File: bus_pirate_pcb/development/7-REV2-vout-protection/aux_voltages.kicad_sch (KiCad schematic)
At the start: 11 parts, among them U18 74LVC2G14

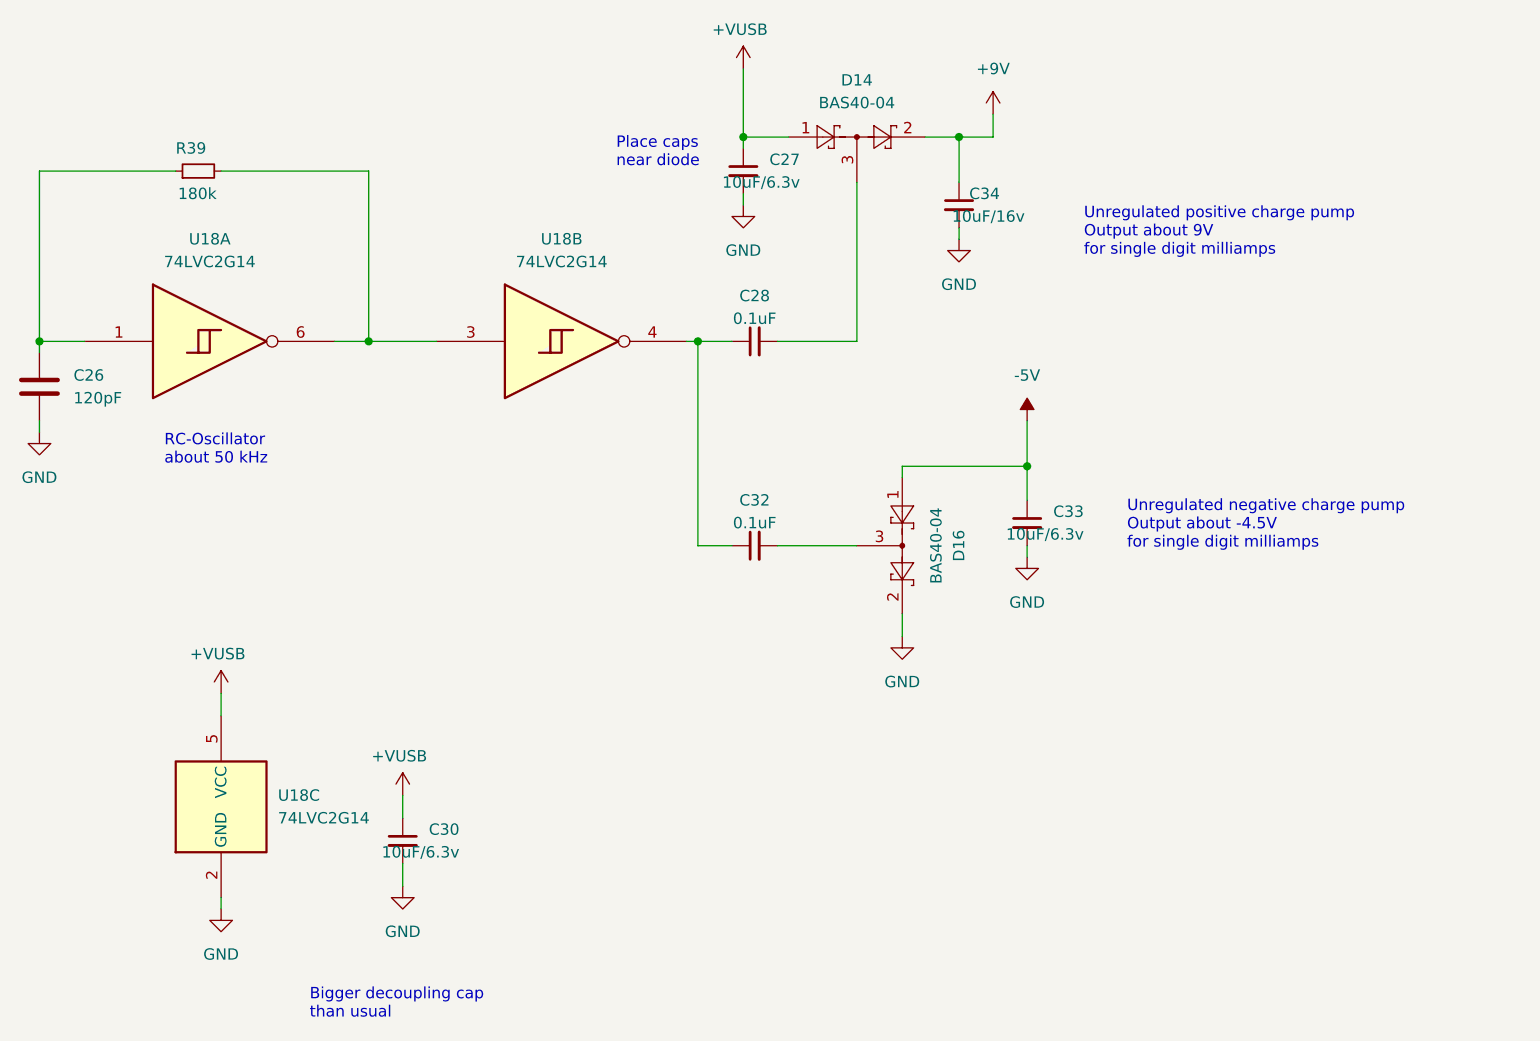
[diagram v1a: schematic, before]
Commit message: 7R2 with vout protection
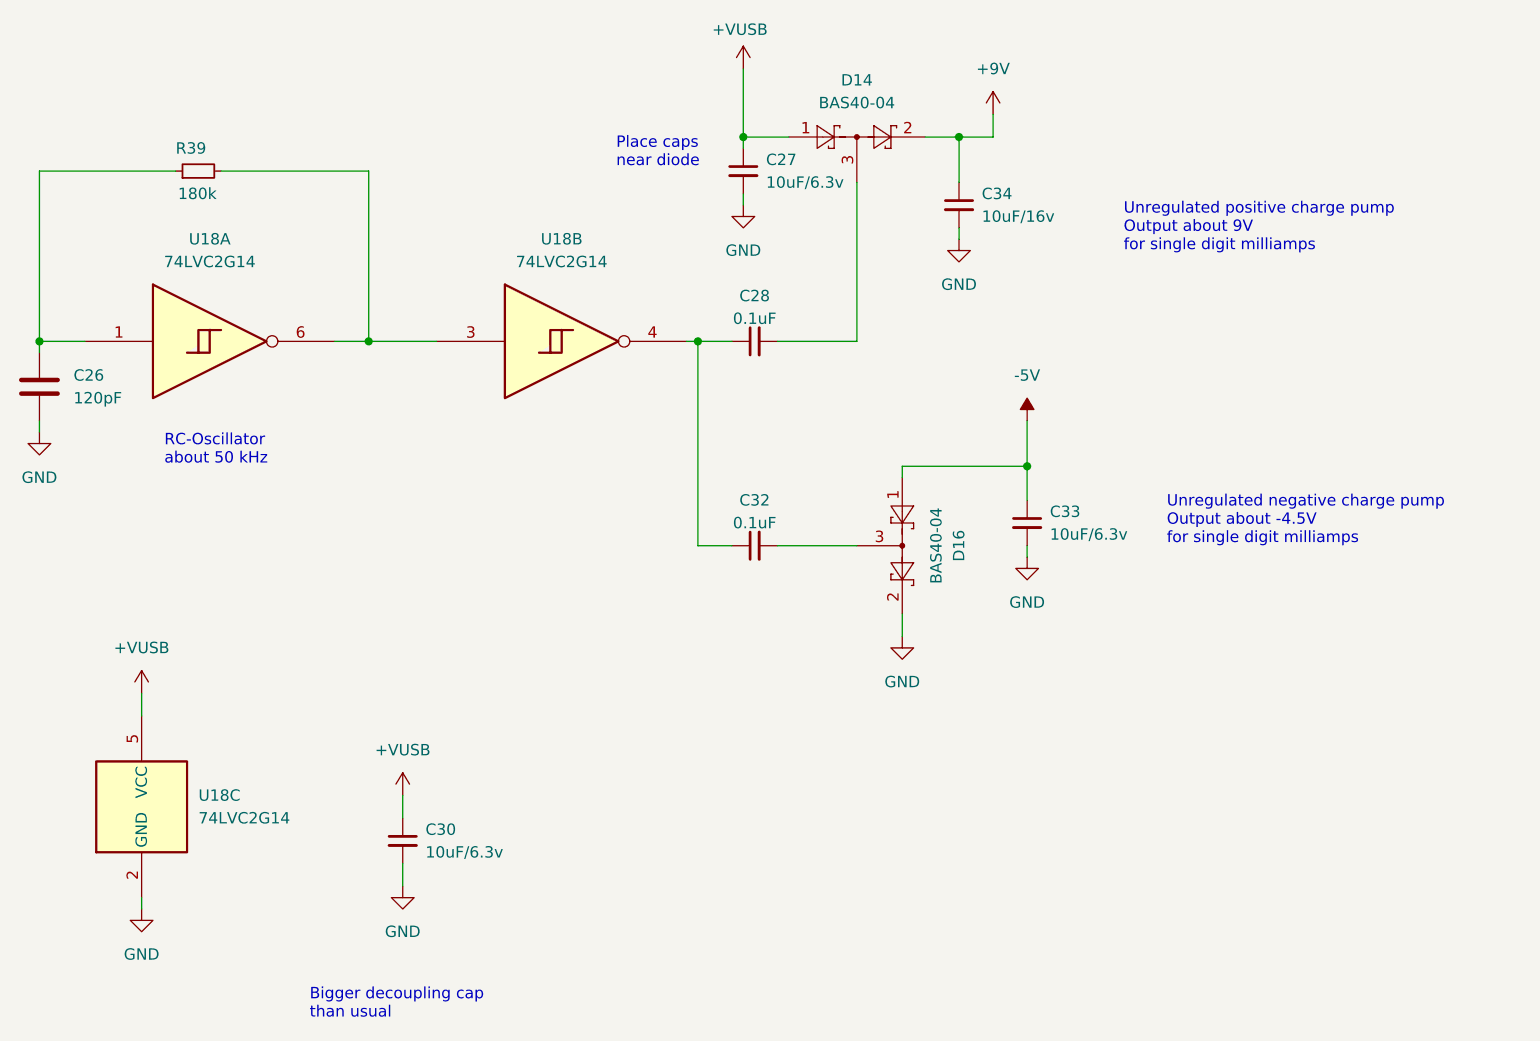
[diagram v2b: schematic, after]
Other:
- moved on the sheet: U18C
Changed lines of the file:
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@@
 	(text "Unregulated positive charge pump\nOutput about 9V\nfor single digit milliamps"
 		(exclude_from_sim no)
-		(at 191.77 88.138 0)
+		(at 196.215 87.63 0)
 		(effects
 			(font
@@
 	(text "Unregulated negative charge pump\nOutput about -4.5V\nfor single digit milliamps"
 		(exclude_from_sim no)
-		(at 196.596 120.904 0)
+		(at 201.041 120.396 0)
 		(effects
 			(font
@@
 	(wire
 		(pts
-			(xy 95.25 162.56) (xy 95.25 163.83)
+			(xy 86.36 162.56) (xy 86.36 163.83)
 		)
 		(stroke
@@
 	(wire
 		(pts
-			(xy 95.25 139.7) (xy 95.25 142.24)
+			(xy 86.36 139.7) (xy 86.36 142.24)
 		)
 		(stroke
@@
 		(on_board yes)
 		(dnp no)
+		(fields_autoplaced yes)
 		(property "Reference" "C30"
-			(at 121.92 154.94 0)
-			(effects
-				(font
-					(size 1.27 1.27)
-				)
-				(justify right)
+			(at 118.11 154.9462 0)
+			(effects
+				(font
+					(size 1.27 1.27)
+				)
+				(justify left)
 			)
 		)
 		(property "Value" "10uF/6.3v"
-			(at 121.92 157.48 0)
-			(effects
-				(font
-					(size 1.27 1.27)
-				)
-				(justify right)
+			(at 118.11 157.4862 0)
+			(effects
+				(font
+					(size 1.27 1.27)
+				)
+				(justify left)
 			)
 		)
@@
 		(on_board yes)
 		(dnp no)
+		(fields_autoplaced yes)
 		(property "Reference" "#PWR0132"
 			(at 115.57 151.13 0)
@@
 		)
 		(property "Value" "+VUSB"
-			(at 115.189 146.7358 0)
+			(at 115.57 146.05 0)
 			(effects
 				(font
@@
 		(on_board yes)
 		(dnp no)
+		(fields_autoplaced yes)
 		(property "Reference" "C33"
-			(at 191.77 119.38 0)
-			(effects
-				(font
-					(size 1.27 1.27)
-				)
-				(justify right)
+			(at 187.96 119.3862 0)
+			(effects
+				(font
+					(size 1.27 1.27)
+				)
+				(justify left)
 			)
 		)
 		(property "Value" "10uF/6.3v"
-			(at 191.77 121.92 0)
-			(effects
-				(font
-					(size 1.27 1.27)
-				)
-				(justify right)
+			(at 187.96 121.9262 0)
+			(effects
+				(font
+					(size 1.27 1.27)
+				)
+				(justify left)
 			)
 		)
@@
 		(on_board yes)
 		(dnp no)
+		(fields_autoplaced yes)
 		(property "Reference" "C34"
-			(at 182.372 83.82 0)
-			(effects
-				(font
-					(size 1.27 1.27)
-				)
-				(justify right)
+			(at 180.34 83.8262 0)
+			(effects
+				(font
+					(size 1.27 1.27)
+				)
+				(justify left)
 			)
 		)
 		(property "Value" "10uF/16v"
-			(at 185.166 86.36 0)
-			(effects
-				(font
-					(size 1.27 1.27)
-				)
-				(justify right)
+			(at 180.34 86.3662 0)
+			(effects
+				(font
+					(size 1.27 1.27)
+				)
+				(justify left)
 			)
 		)
@@
 		(lib_name "GND_8")
 		(lib_id "power:GND")
-		(at 95.25 163.83 0)
+		(at 86.36 163.83 0)
 		(unit 1)
 		(exclude_from_sim no)
@@
 		(fields_autoplaced yes)
 		(property "Reference" "#PWR0128"
-			(at 95.25 170.18 0)
+			(at 86.36 170.18 0)
 			(effects
 				(font
@@
 		)
 		(property "Value" "GND"
-			(at 95.25 168.91 0)
+			(at 86.36 168.91 0)
 			(effects
 				(font
@@
 		)
 		(property "Footprint" ""
-			(at 95.25 163.83 0)
+			(at 86.36 163.83 0)
 			(effects
 				(font
@@
 		)
 		(property "Datasheet" ""
-			(at 95.25 163.83 0)
+			(at 86.36 163.83 0)
 			(effects
 				(font
@@
 		)
 		(property "Description" "Power symbol creates a global label with name \"GND\" , ground"
-			(at 95.25 163.83 0)
+			(at 86.36 163.83 0)
 			(effects
 				(font
@@
 		(on_board yes)
 		(dnp no)
+		(fields_autoplaced yes)
 		(property "Reference" "C27"
-			(at 160.02 80.01 0)
-			(effects
-				(font
-					(size 1.27 1.27)
-				)
-				(justify right)
+			(at 156.21 80.0162 0)
+			(effects
+				(font
+					(size 1.27 1.27)
+				)
+				(justify left)
 			)
 		)
 		(property "Value" "10uF/6.3v"
-			(at 160.02 82.55 0)
-			(effects
-				(font
-					(size 1.27 1.27)
-				)
-				(justify right)
+			(at 156.21 82.5562 0)
+			(effects
+				(font
+					(size 1.27 1.27)
+				)
+				(justify left)
 			)
 		)
@@
 	(symbol
 		(lib_id "dp-power:+VUSB")
-		(at 95.25 139.7 0)
+		(at 86.36 139.7 0)
 		(unit 1)
 		(exclude_from_sim no)
@@
 		(on_board yes)
 		(dnp no)
+		(fields_autoplaced yes)
 		(property "Reference" "#PWR0121"
-			(at 95.25 139.7 0)
+			(at 86.36 139.7 0)
 			(effects
 				(font
@@
 		)
 		(property "Value" "+VUSB"
-			(at 94.869 135.3058 0)
+			(at 86.36 134.62 0)
 			(effects
 				(font
@@
 		)
 		(property "Footprint" ""
-			(at 95.25 139.7 0)
+			(at 86.36 139.7 0)
 			(effects
 				(font
@@
 		)
 		(property "Datasheet" ""
-			(at 95.25 139.7 0)
+			(at 86.36 139.7 0)
 			(effects
 				(font
@@
 		)
 		(property "Description" ""
-			(at 95.25 139.7 0)
+			(at 86.36 139.7 0)
 			(effects
 				(font
@@
 		(on_board yes)
 		(dnp no)
-		(fields_autoplaced yes)
 		(property "Reference" "#PWR0140"
 			(at 185.42 113.03 0)
@@
 	(symbol
 		(lib_id "74xGxx:74LVC2G14")
-		(at 95.25 152.4 0)
+		(at 86.36 152.4 0)
 		(unit 3)
 		(exclude_from_sim no)
@@
 		(fields_autoplaced yes)
 		(property "Reference" "U18"
-			(at 101.6 151.1299 0)
+			(at 92.71 151.1299 0)
 			(effects
 				(font
@@
 		)
 		(property "Value" "74LVC2G14"
-			(at 101.6 153.6699 0)
+			(at 92.71 153.6699 0)
 			(effects
 				(font
@@
 		)
 		(property "Footprint" "Package_TO_SOT_SMD:SOT-363_SC-70-6"
-			(at 95.25 152.4 0)
+			(at 86.36 152.4 0)
 			(effects
 				(font
@@
 		)
 		(property "Datasheet" "https://www.ti.com/lit/ds/symlink/sn74lvc2g14.pdf"
-			(at 95.25 152.4 0)
+			(at 86.36 152.4 0)
 			(effects
 				(font
@@
 		)
 		(property "Description" "Dual NOT Gate, Schmitt Triggered, Low-Voltage CMOS"
-			(at 95.25 152.4 0)
+			(at 86.36 152.4 0)
 			(effects
 				(font
@@
 		)
 		(property "Description_1" ""
-			(at 95.25 152.4 0)
+			(at 86.36 152.4 0)
 			(effects
 				(font
@@
 		)
 		(property "MAXIMUM_PACKAGE_HEIGHT" ""
-			(at 95.25 152.4 0)
+			(at 86.36 152.4 0)
 			(effects
 				(font
@@
 		)
 		(property "PARTREV" ""
-			(at 95.25 152.4 0)
+			(at 86.36 152.4 0)
 			(effects
 				(font
@@
 		)
 		(property "STANDARD" ""
-			(at 95.25 152.4 0)
-			(effects
-				(font
+			(at 86.36 152.4 0)
+			(effects
+				(font
